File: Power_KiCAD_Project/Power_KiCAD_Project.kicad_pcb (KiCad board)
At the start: 4 copper layers, 170 x 87.2 mm, 76 parts, among them J1 XT60-M, J10 DB37_Female, J11 DB37_Female, J12 DB37_Female, J2 XT60-M, J3 XT60-M, J4 XT60-M, J5 XT60-M, J6 Barrel_Jack, J7 DB37_Female, J8 DB37_Female, J9 DB37_Female, Q1 CSD17501Q5A, Q2 BSS84PH6327XTSA2, Q3 CSD17501Q5A, SW1 Reboot, U1 MCP9808_MSOP, U2 MCP9808_MSOP, U3 BQ76920PW, U5 LM2678SX-5.0/NOPB, U6 LM2678SX-3.3/NOPB, Y1 Crystal

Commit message: pcb finished
pcb is done. 3am kicad be like
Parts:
- removed C30, C31, C32, C33, C34: 100nF, Capacitor_SMD:C_0603_1608Metric
- removed J10, J11, J12, J8, J9: DB37_Female, Connector_Dsub:DSUB-15_Female_Horizontal_P2.77x2.84mm_EdgePinOffset14.56mm_Housed_MountingHolesOffset8.20mm
- removed the R9 at (211.2, 132.6)
- added C21: 35SVPF82M, SamacSys_Parts:16SVPT560M, F.Cu at (95.8, 101.8)
- added C22: 35SVPF82M, SamacSys_Parts:16SVPT560M, F.Cu at (95.8, 112.3)
- added C27: 16SVP330M, SamacSys_Parts:16SVF1000M, F.Cu at (95.8, 72.8)
- added C28: 6SVPC330M, SamacSys_Parts:16SVF180M, F.Cu at (94.8, 92.2)
- added IC1: STM32L562VET6Q, SamacSys_Parts:QFP50P1600X1600X160-100N, F.Cu at (129.0, 112.0)
- added L1: SRP1270-8R2M, SamacSys_Parts:INDPM137129X700N, F.Cu at (147.0, 120.0)
- added L2: MSS1210-153MEB, MSS1210-153MEB:IND_MSS1210-153MEB, F.Cu at (115.8, 138.8)
- added VR1: T93YA103KT20, SamacSys_Parts:T93YA5K10, F.Cu at (123.8, 93.5)
- C23, C24: footprint Capacitor_SMD:C_0805_2012Metric -> SamacSys_Parts:CAPC2012X88N
- C25, C26: footprint Capacitor_SMD:C_0805_2012Metric -> SamacSys_Parts:CAPC2012X75N; moved to B.Cu
- J1, J2, J3, J4, J5: moved to B.Cu
- J6: value Barrel_Jack -> PJ-102AH; footprint Connector_BarrelJack:BarrelJack_CUI_PJ-036AH-SMT_Horizontal -> SamacSys_Parts:PJ-102AH; moved to B.Cu
- J7: value DB37_Female -> L717SDC37P1ACH4F; footprint Connector_Dsub:DSUB-15_Female_Horizontal_P2.77x2.84mm_EdgePinOffset14.56mm_Housed_MountingHolesOffset8.20mm -> SamacSys_Parts:L717SDC37P1ACH4F; moved to B.Cu
- moved J5 131.4 mm to (146.8, 72.0)
- moved J3 122.1 mm to (146.8, 89.8)
- moved R15 119.5 mm to (109.5, 76.8), turned to 180 degrees
- moved U2 116.7 mm to (110.6, 121.4), turned to 180 degrees
- moved J4 116.2 mm to (146.8, 80.8)
- moved C17 116.1 mm to (136.0, 122.0)
- moved C13 114.8 mm to (106.5, 83.0), turned to 270 degrees
- moved R14 114.7 mm to (103.6, 92.0)
- moved C20 114.2 mm to (136.0, 131.0)
- moved R8 112.1 mm to (109.5, 92.8)
- moved C16 111.5 mm to (136.0, 124.3)
- moved Q2 111.3 mm to (102.5, 82.2), turned to 90 degrees
- moved D4 108.6 mm to (139.2, 119.9), turned to 90 degrees
- moved Q3 107.5 mm to (108.5, 70.8), turned to 270 degrees
- moved C18 106.8 mm to (136.0, 126.5)
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- renumbered D4 to D3, D3 to D4, R11 to R10, R12 to R11, R13 to R12, R14 to R13, R15 to R14, R16 to R15, R18 to R16, R10 to R9, U5 to U4, U6 to U5
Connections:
- net /Sheet61A88F08/Fire renamed /Sheet61D3585D/Fire
- net /Sheet61A88F08/t_miso renamed /Sheet61D3585D/t_miso
- C11 pad 2: +3V3 -> Net-(C11-Pad2)
- D1 pad 2: +3V3 -> Net-(C11-Pad2)
- D6 pad 1: Net-(D6-Pad1) -> /Pack-
- J3 pad 1: Net-(J3-Pad1) -> /PACK_M3
- J6 pad 3: (no net) -> Net-(J6-Pad3)
- U3 pad 8: +3V3 -> Net-(C11-Pad2)
- U5 pad 6: +3V3 -> Net-(L1-Pad1)
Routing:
- net +3V3: track 0.00 -> 354.6 mm, vias 0 -> 3
- net +5V: track 0.00 -> 321.2 mm
- net /Pack-: track 0.00 -> 283.6 mm, vias 0 -> 3
- net /PACK_M5: track 0.00 -> 201.7 mm, vias 0 -> 2
- net GND: track 0.00 -> 92.8 mm, vias 0 -> 2
- net /SWCLK: track 0.00 -> 66.0 mm, vias 0 -> 1
- net /SWDIO: track 0.00 -> 59.8 mm, vias 0 -> 1
- net /Alert_sda: track 0.00 -> 56.7 mm, vias 0 -> 1
- net Net-(L1-Pad1): track 0.00 -> 54.5 mm
- net /Alert_active: track 0.00 -> 54.3 mm, vias 0 -> 1
- net /Alert_scl: track 0.00 -> 53.5 mm, vias 0 -> 1
- net /LiPo Pack Monitor/VC1: track 0.00 -> 53.2 mm, vias 0 -> 2
- net /I2C_SCL: track 0.00 -> 46.8 mm, vias 0 -> 2
- net Net-(C26-Pad2): track 0.00 -> 43.8 mm, vias 0 -> 2
- net /I2C_SDA: track 0.00 -> 40.3 mm, vias 0 -> 2
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- added copper zone on ground_2, net /Pack-
- added copper zone on ground, net GND
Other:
- board size 170 x 87.2 mm -> 80 x 87.2 mm

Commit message: Changes to PCB
Bunch of changes to layout with components on the other side
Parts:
- C21, C22, C24, C27, C28, L1, L2, SW1, VR1: moved to B.Cu
- C25, C26: moved to F.Cu
- moved C24 23.9 mm to (95.5, 95.2), turned to 180 degrees
- moved C27 4.01 mm to (99.8, 73.0), turned to 90 degrees
- moved C28 3.13 mm to (96.2, 89.5), turned to 90 degrees
- moved C22 1.52 mm to (97.2, 112.0), turned to 180 degrees
- moved C21 1.50 mm to (97.2, 101.8), turned to 180 degrees
- moved VR1 0.56 mm to (123.2, 93.2), turned to 0 degrees
- turned L1 to 270 degrees
- turned SW1 to 270 degrees
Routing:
- net +5V: track 321.2 -> 149.4 mm
- net +3V3: track 354.6 -> 299.4 mm
- net /Pack-: track 283.6 -> 264.5 mm
- net Net-(L1-Pad1): track 54.5 -> 67.5 mm, vias 0 -> 1
- net Net-(C26-Pad2): track 43.8 -> 36.0 mm
- net /PACK_M5: track 201.7 -> 205.6 mm, vias 2 -> 1
- net Net-(C26-Pad1): track 7.35 -> 10.4 mm, vias 1 -> 0
- net /LiPo Pack Monitor/VC1: track 53.2 -> 55.5 mm, vias 2 -> 3
- net Net-(R10-Pad2): track 25.5 -> 23.2 mm, vias 2 -> 1
- net Net-(C25-Pad2): track 38.4 -> 36.3 mm, vias 2 -> 1
- net /SWCLK: track 66.0 -> 67.9 mm
- net Net-(C25-Pad1): track 8.27 -> 7.61 mm, vias 1 -> 0
- net /SWDIO: track 59.8 -> 60.3 mm
- net (no net): vias 2 -> 0

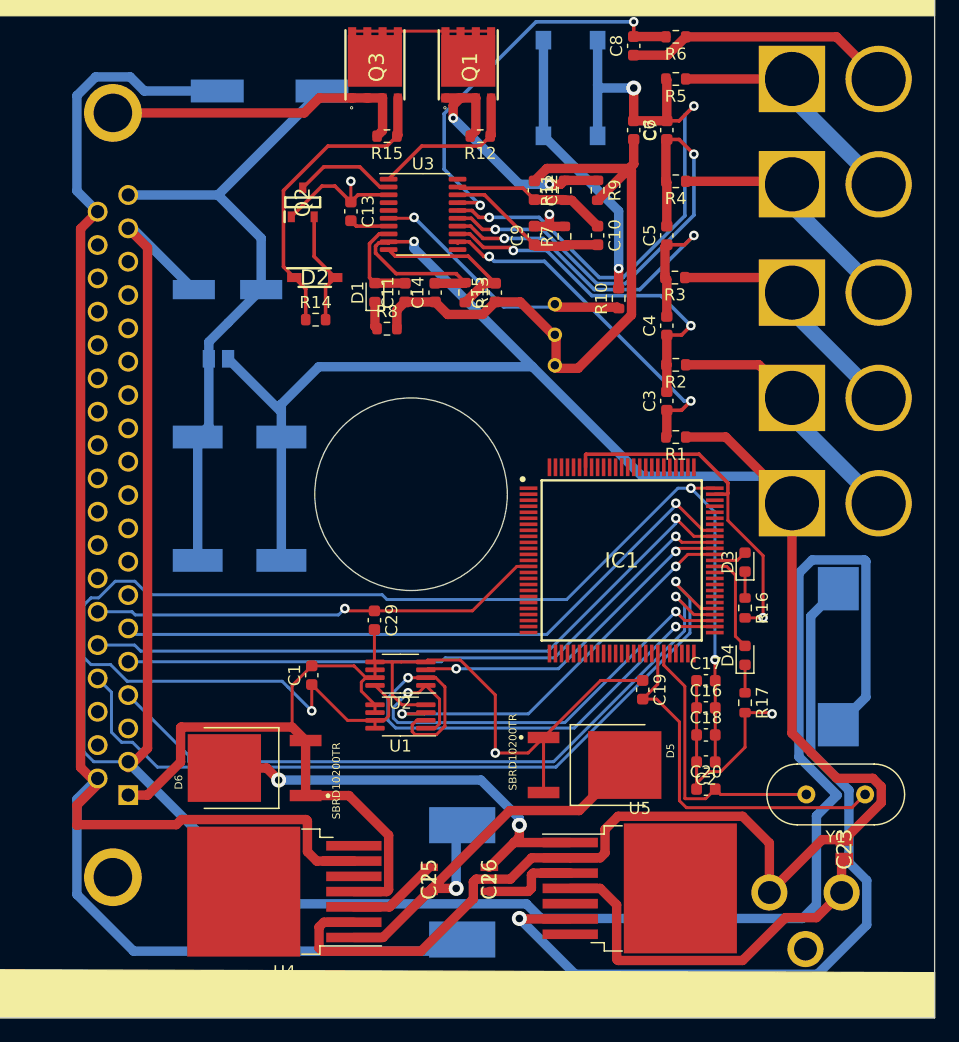
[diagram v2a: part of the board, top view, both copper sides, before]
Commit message: updated pcb
more updates because stuff was a bit too far away from their connected components
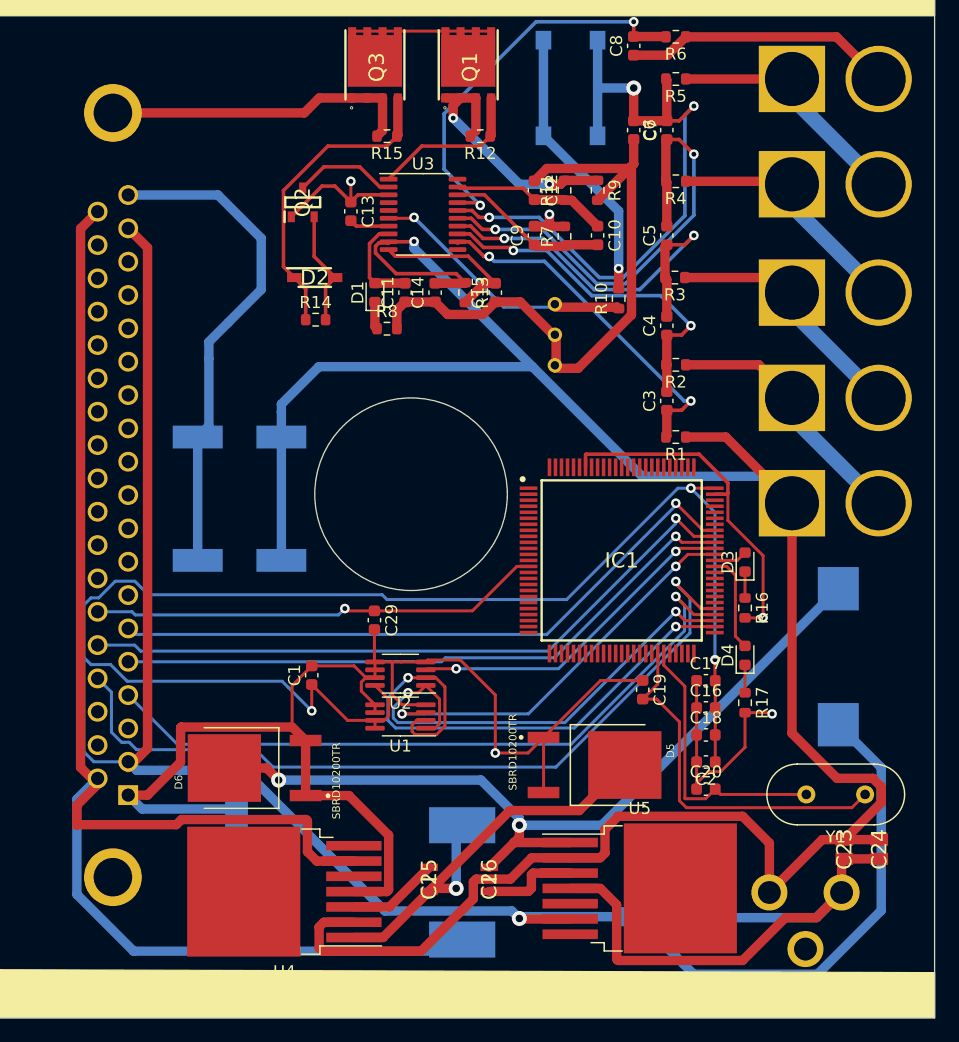
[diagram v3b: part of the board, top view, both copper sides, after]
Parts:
- C24: moved to F.Cu
- moved C24 68.4 mm to (150.4, 136.0), turned to 270 degrees
- moved C27 64.1 mm to (97.0, 137.0), turned to 180 degrees
- moved C28 63.8 mm to (133.0, 141.6)
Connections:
- L1 pad 1: Net-(L1-Pad1) -> Net-(C26-Pad2)
- U5 pad 6: Net-(L1-Pad1) -> +3V3
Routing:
- net Net-(L1-Pad1): track 67.5 -> 0.00 mm, vias 1 -> 0
- net Net-(C26-Pad2): track 36.0 -> 70.6 mm
- net +3V3: track 299.4 -> 272.6 mm, vias 3 -> 4
- net +5V: track 149.4 -> 130.0 mm
- net /Pack-: track 264.5 -> 277.0 mm
- net /PACK_M5: track 205.6 -> 202.2 mm
- net /SWDIO: track 60.3 -> 58.8 mm
